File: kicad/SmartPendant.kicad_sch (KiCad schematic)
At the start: 52 parts, among them J1 UART, J2 ST-LINK, J3 Conn_01x05, J4 TYPE-C16PIN, J5 Display, Q2 MMBT3904, U1 WEACT BLACKPILL F4X1, U2 AMS1117-3.3, U3 MB85RC256VPNF

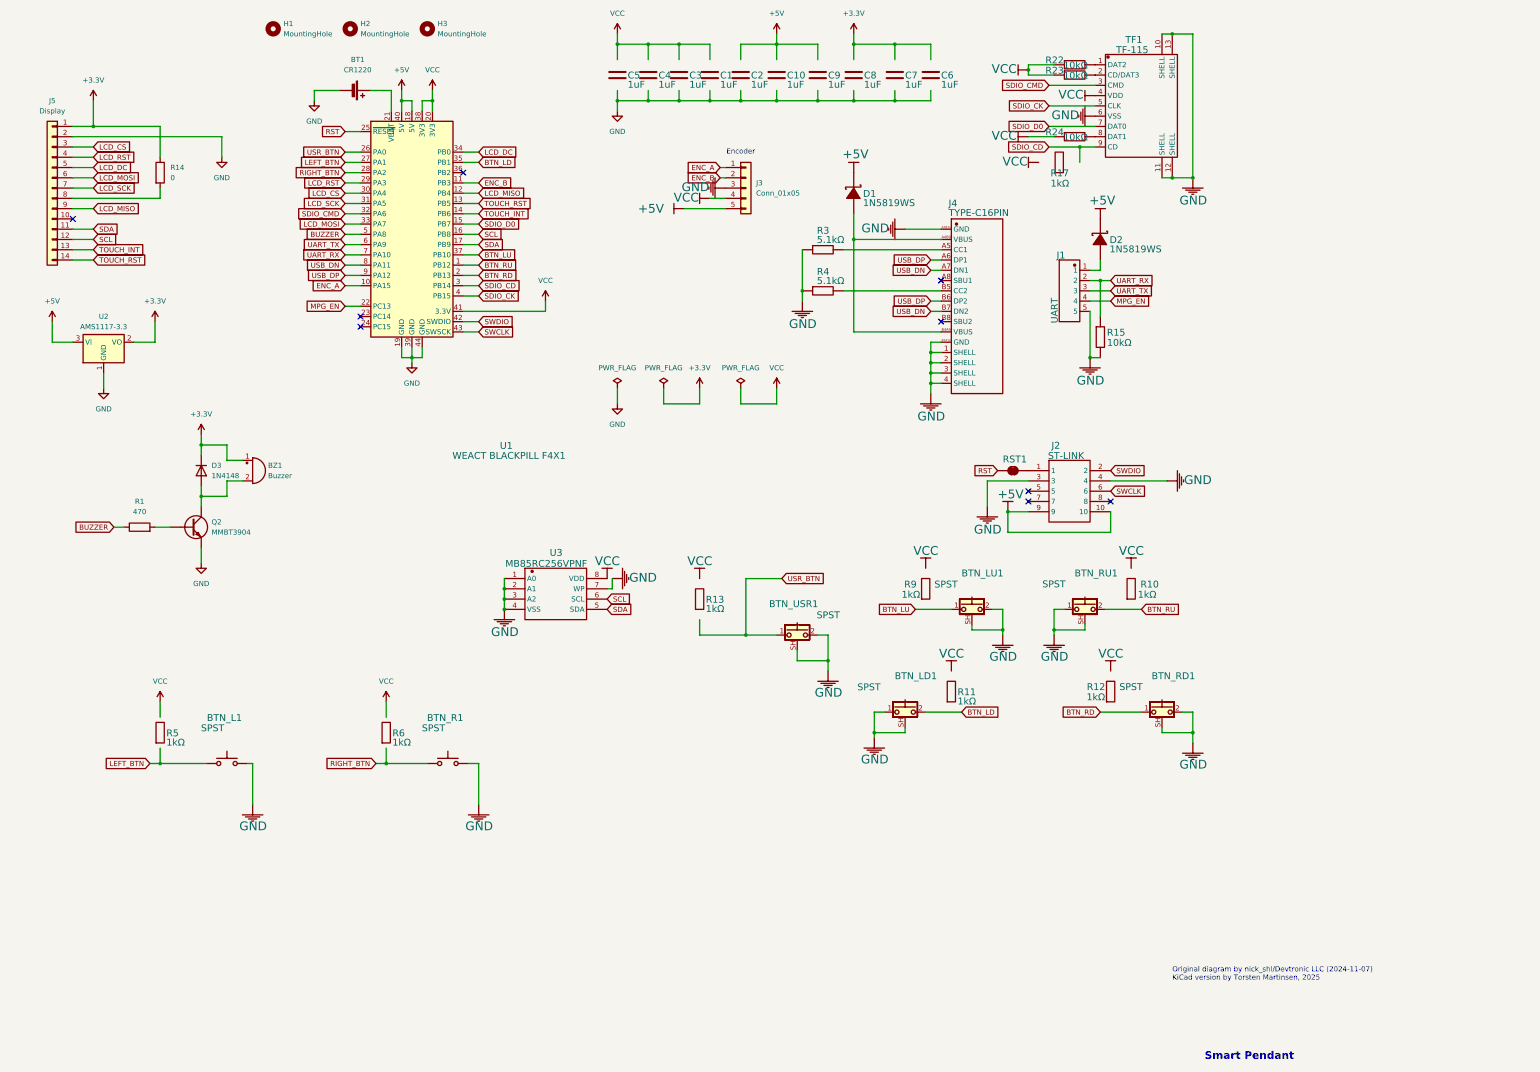
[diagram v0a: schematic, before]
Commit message: Update rest of power symbols.
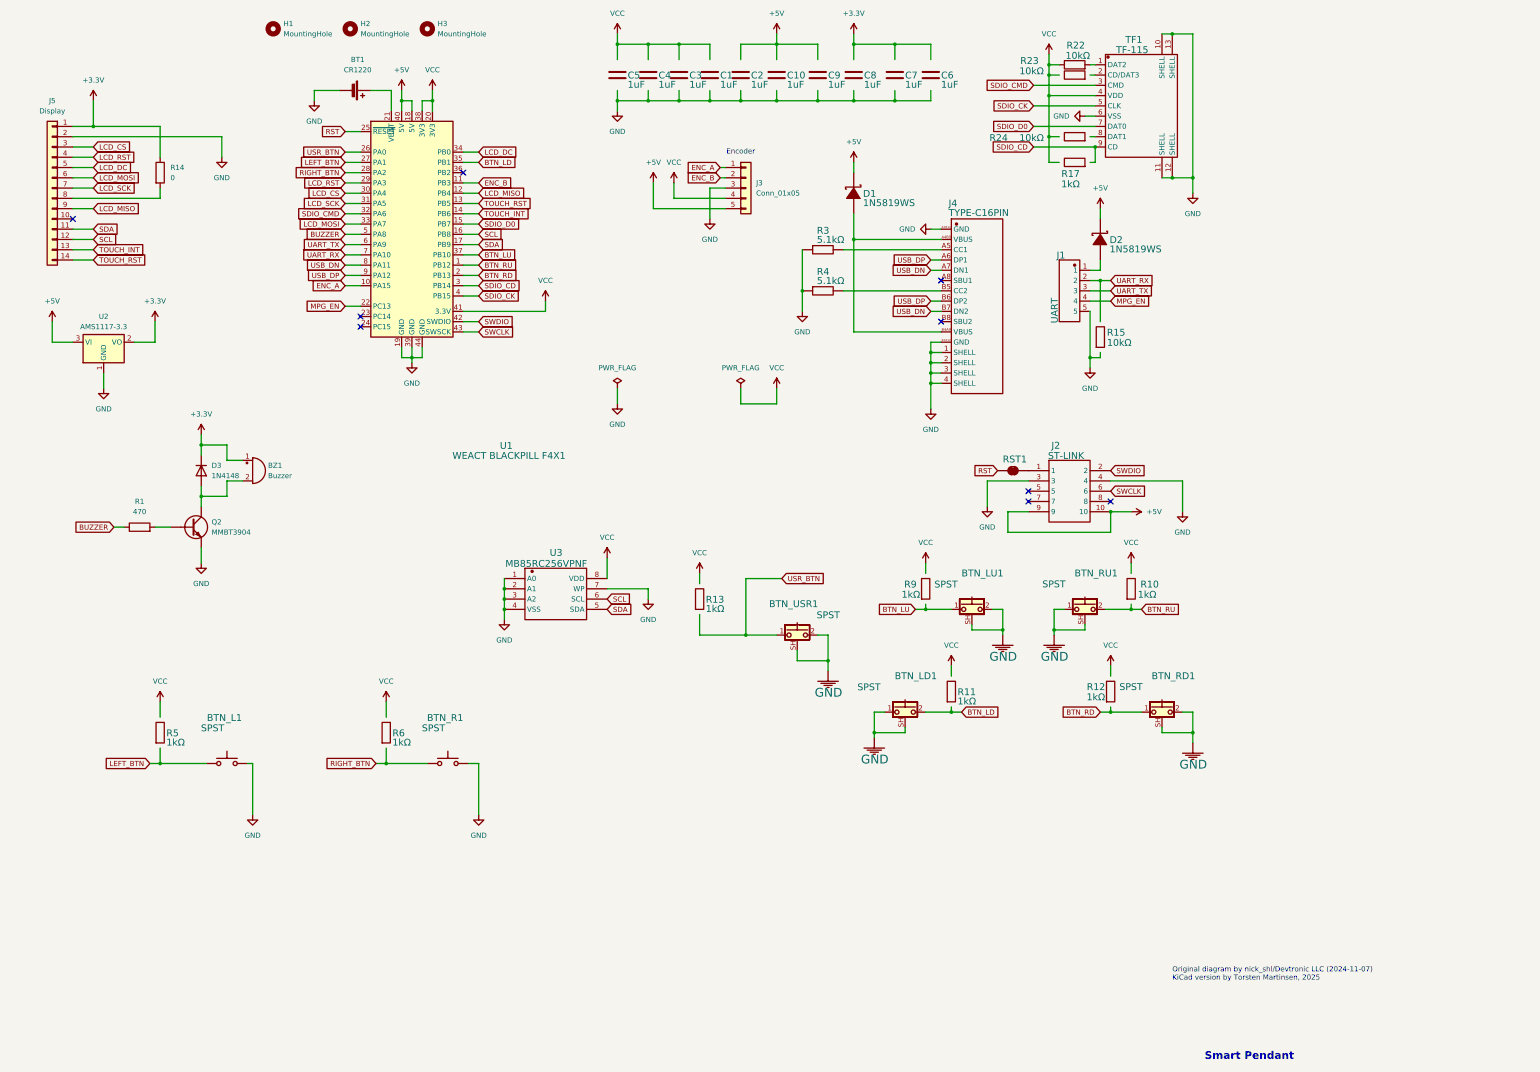
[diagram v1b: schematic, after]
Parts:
- R15: symbol 0805W8F1002T5E_13 -> Device:R
- R22: symbol 0805W8F1002T5E_14 -> Device:R
- R23: symbol 0805W8F1002T5E_15 -> Device:R
- R24: symbol 0805W8F1002T5E_16 -> Device:R
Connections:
- net GND: no longer R15.2
- net UART_RX: no longer R15.1
- net VCC: no longer R23.1, R24.1
- net at TF1.8 (DAT1): no longer R24.2
- net at TF1.2 (CD/DAT3): no longer R23.2
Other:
- moved on the sheet: R17

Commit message: Add footprints, initial outline.
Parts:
- removed H3: MountingHole, MountingHole:MountingHole_3.2mm_M3, symbol Mechanical:MountingHole
- removed Q2: MMBT3904, symbol Device:Q_NPN
- added Q1: MMBT3904, Package_TO_SOT_SMD:SOT-23, symbol Transistor_BJT:MMBT3904
- BT1: footprint (none) -> Custom:CR1220_Battery_Holder
- J5: footprint Connector_PinSocket_2.54mm:PinSocket_1x14_P2.54mm_Vertical_SMD_Pin1Left -> Custom:PinSocket_1x14_P2.54mm_Vertical_SMD_Pin1Left_TH
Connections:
- net GND: now also Q1.2 (E)
- net at R1.2: now also Q1.1 (B)
- net at BZ1.2 (-), D3.2 (A): now also Q1.3 (C)
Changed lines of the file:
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@@
 	)
 	(symbol
-		(lib_id "Mechanical:MountingHole")
-		(at 118.11 22.86 0)
-		(unit 1)
-		(exclude_from_sim no)
-		(in_bom no)
-		(on_board yes)
-		(dnp no)
-		(fields_autoplaced yes)
-		(property "Reference" "H3"
-			(at 120.65 21.5899 0)
-			(effects
-				(font
-					(size 1.27 1.27)
-				)
-				(justify left)
-			)
-		)
-		(property "Value" "MountingHole"
-			(at 120.65 24.1299 0)
-			(effects
-				(font
-					(size 1.27 1.27)
-				)
-				(justify left)
-			)
-		)
-		(property "Footprint" "MountingHole:MountingHole_3.2mm_M3"
-			(at 118.11 22.86 0)
-			(effects
-				(font
-					(size 1.27 1.27)
-				)
-				(hide yes)
-			)
-		)
-		(property "Datasheet" "~"
-			(at 118.11 22.86 0)
-			(effects
-				(font
-					(size 1.27 1.27)
-				)
-				(hide yes)
-			)
-		)
-		(property "Description" "Mounting Hole without connection"
-			(at 118.11 22.86 0)
-			(effects
-				(font
-					(size 1.27 1.27)
-				)
-				(hide yes)
-			)
-		)
-		(instances
-			(project ""
-				(path "/78cb6519-38e9-49e2-a9df-0cb5fdb5035f"
-					(reference "H3")
-					(unit 1)
-				)
-			)
-		)
-	)
-	(symbol
 		(lib_id "TYPE-C16PIN")
 		(at 254 91.44 0)
@@
 	)
 	(symbol
-		(lib_id "Device:Q_NPN")
-		(at 59.69 146.05 0)
-		(unit 1)
-		(exclude_from_sim no)
-		(in_bom yes)
-		(on_board yes)
-		(dnp no)
-		(fields_autoplaced yes)
-		(property "Reference" "Q2"
-			(at 64.77 144.7799 0)
-			(effects
-				(font
-					(size 1.27 1.27)
-				)
-				(justify left)
-			)
-		)
-		(property "Value" "MMBT3904"
-			(at 64.77 147.3199 0)
-			(effects
-				(font
-					(size 1.27 1.27)
-				)
-				(justify left)
-			)
-		)
-		(property "Footprint" ""
-			(at 64.77 143.51 0)
-			(effects
-				(font
-					(size 1.27 1.27)
-				)
-				(hide yes)
-			)
-		)
-		(property "Datasheet" "~"
-			(at 59.69 146.05 0)
-			(effects
-				(font
-					(size 1.27 1.27)
-				)
-				(hide yes)
-			)
-		)
-		(property "Description" "NPN bipolar junction transistor"
-			(at 59.69 146.05 0)
-			(effects
-				(font
-					(size 1.27 1.27)
-				)
-				(hide yes)
-			)
-		)
-		(pin "C"
-		)
-		(pin "B"
-		)
-		(pin "E"
-		)
-		(instances
-			(project ""
-				(path "/78cb6519-38e9-49e2-a9df-0cb5fdb5035f"
-					(reference "Q2")
-					(unit 1)
-				)
-			)
-		)
-	)
-	(symbol
 		(lib_id "Device:R")
 		(at 278.13 49.53 90)
@@
 			)
 		)
-		(property "Footprint" "Connector_PinSocket_2.54mm:PinSocket_1x14_P2.54mm_Vertical_SMD_Pin1Left"
+		(property "Footprint" "Custom:PinSocket_1x14_P2.54mm_Vertical_SMD_Pin1Left_TH"
 			(at 25.4 62.23 0)
 			(effects
@@
 			)
 		)
-		(property "Footprint" ""
+		(property "Footprint" "Custom:CR1220_Battery_Holder"
 			(at 100.584 38.1 90)
 			(effects
@@
 					(unit 1)
 				)
+			)
+		)
+	)
+	(symbol
+		(lib_id "Transistor_BJT:MMBT3904")
+		(at 59.69 146.05 0)
+		(unit 1)
+		(exclude_from_sim no)
+		(in_bom yes)
+		(on_board yes)
+		(dnp no)
+		(fields_autoplaced yes)
+		(property "Reference" "Q1"
+			(at 64.77 144.7799 0)
+			(effects
+				(font
+					(size 1.27 1.27)
+				)
+				(justify left)
+			)
+		)
+		(property "Value" "MMBT3904"
+			(at 64.77 147.3199 0)
+			(effects
+				(font
+					(size 1.27 1.27)
+				)
+				(justify left)
+			)
+		)
+		(property "Footprint" "Package_TO_SOT_SMD:SOT-23"
+			(at 64.77 147.955 0)
+			(effects
+				(font
+					(size 1.27 1.27)
+					(italic yes)
+				)
+				(justify left)
+				(hide yes)
+			)
+		)
+		(property "Datasheet" "https://www.onsemi.com/pdf/datasheet/pzt3904-d.pdf"
+			(at 59.69 146.05 0)
+			(effects
+				(font
+					(size 1.27 1.27)
+				)
+				(justify left)
+				(hide yes)
+			)
+		)
+		(property "Description" "0.2A Ic, 40V Vce, Small Signal NPN Transistor, SOT-23"
+			(at 59.69 146.05 0)
+			(effects
+				(font
+					(size 1.27 1.27)
+				)
+				(hide yes)
+			)
+		)
+		(pin "1"
+		)
+		(pin "3"
+		)
+		(pin "2"
+		)
+		(instances
+			(project ""
+				(path "/78cb6519-38e9-49e2-a9df-0cb5fdb5035f"
+					(reference "Q1")
+					(unit 1)
+				)

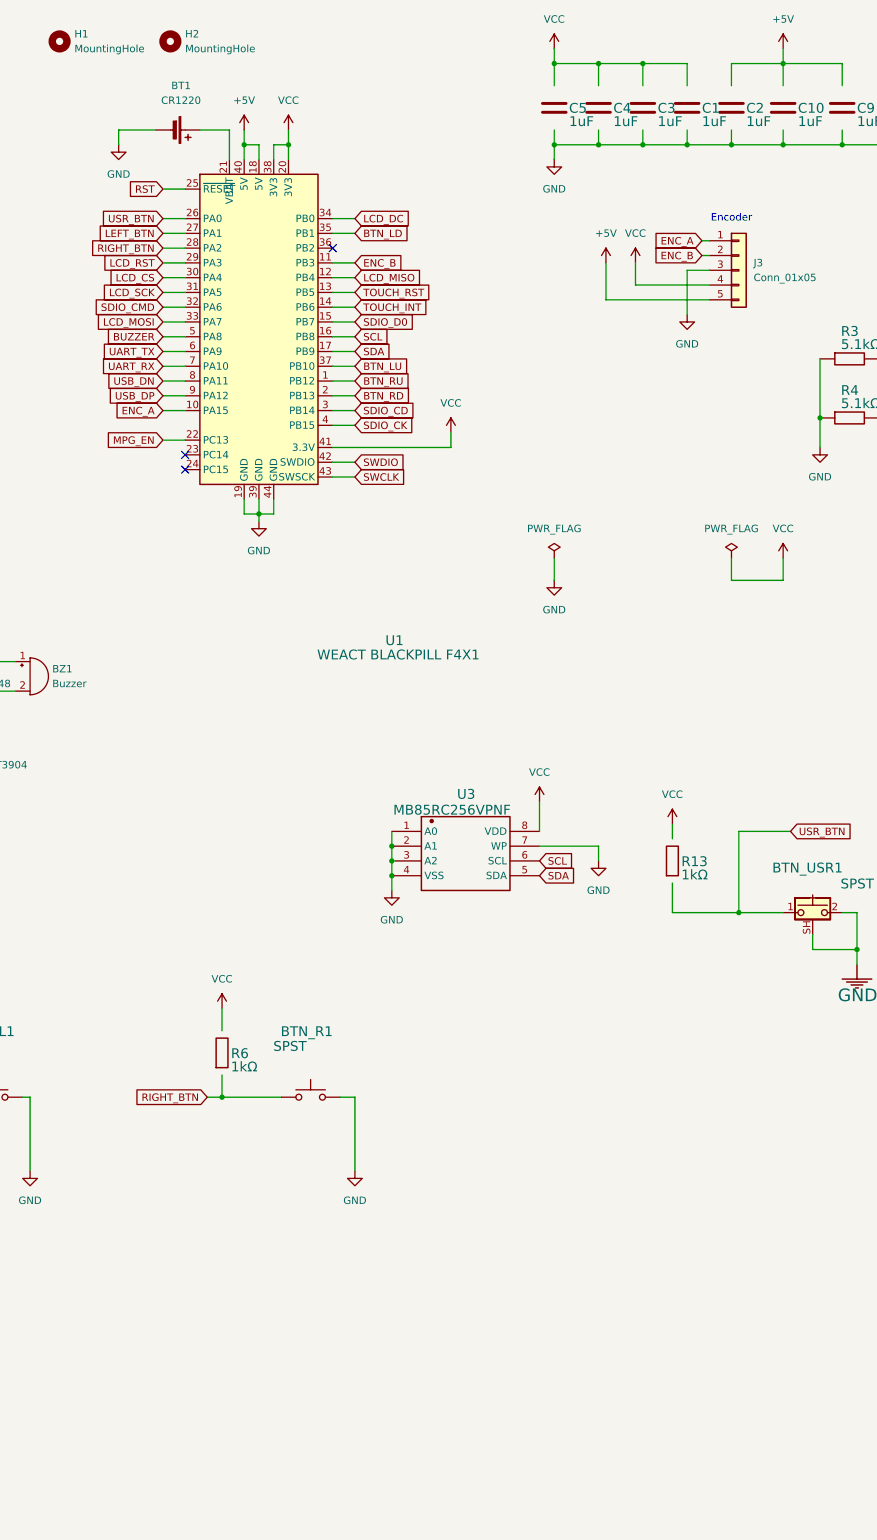
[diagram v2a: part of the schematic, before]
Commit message: Fix some footprint issues.
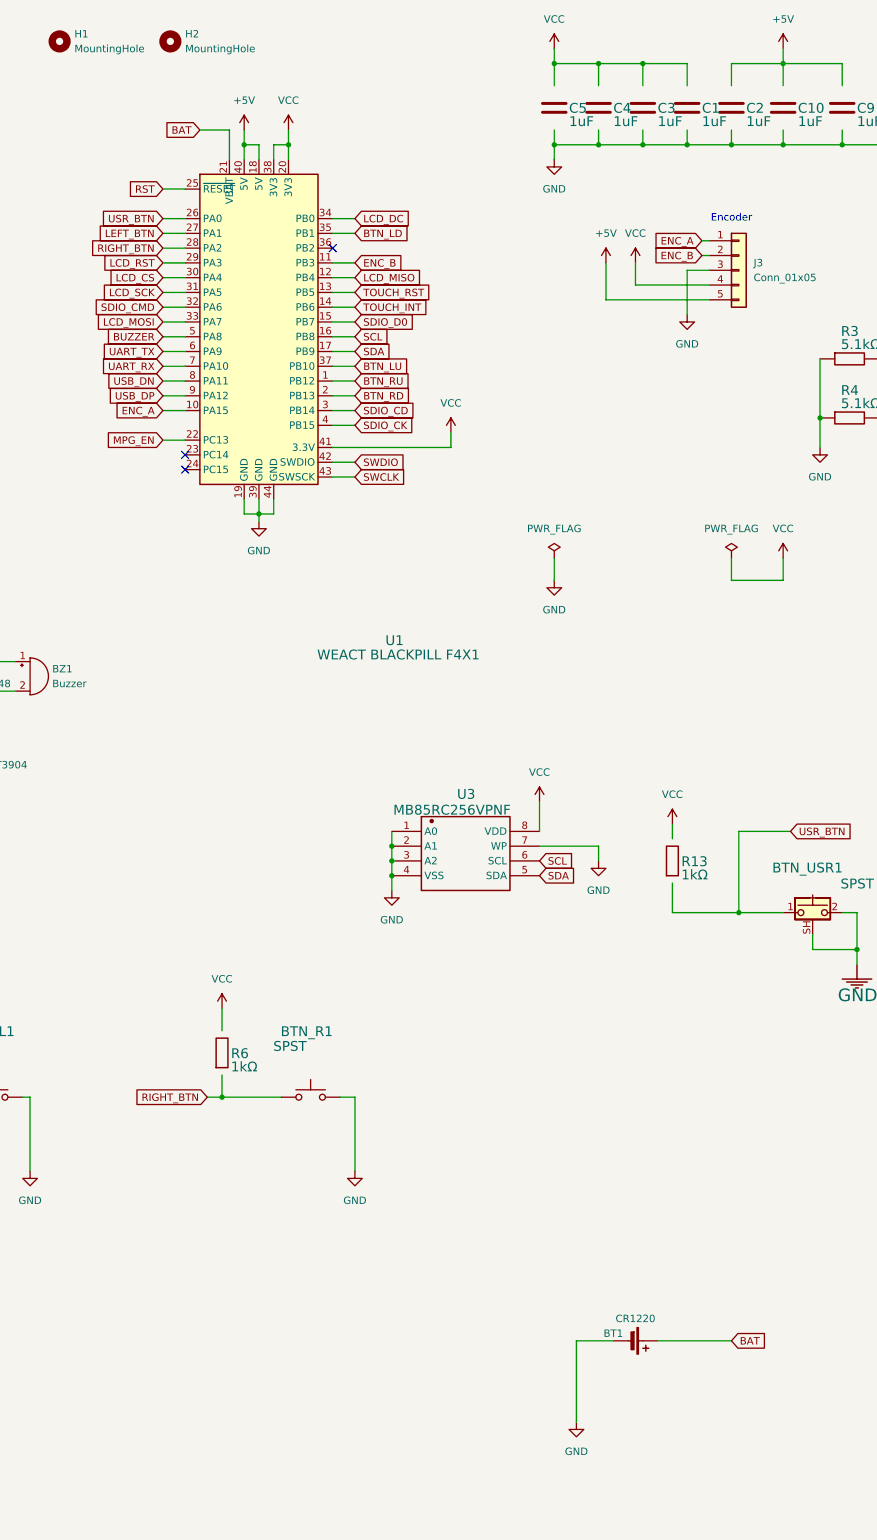
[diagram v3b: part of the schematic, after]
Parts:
- BTN_LD1, BTN_LU1, BTN_RD1, BTN_RU1, BTN_USR1: footprint SmartPendant:SMD_Push_Side_button_3x6x3.5mm -> Custom:SMD_Push_Side_button_3x6x3.5mm
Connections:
- net BAT: now reaches BT1.1 (+), U1.21 (VBAT)
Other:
- moved on the sheet: BT1
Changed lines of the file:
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@@
 	(wire
 		(pts
+			(xy 182.88 246.38) (xy 195.58 246.38)
+		)
+		(stroke
+			(width 0)
+			(type default)
+		)
+	)
+	(wire
+		(pts
 			(xy 307.34 59.69) (xy 302.26 59.69)
 		)
@@
 	(wire
 		(pts
-			(xy 90.17 38.1) (xy 90.17 40.64)
+			(xy 283.21 55.88) (xy 283.21 52.07)
 		)
 		(stroke
@@
 	(wire
 		(pts
-			(xy 283.21 55.88) (xy 283.21 52.07)
+			(xy 114.3 104.14) (xy 114.3 105.41)
 		)
 		(stroke
@@
 	(wire
 		(pts
-			(xy 114.3 104.14) (xy 114.3 105.41)
+			(xy 287.02 142.24) (xy 287.02 147.32)
 		)
 		(stroke
@@
 	(wire
 		(pts
-			(xy 287.02 142.24) (xy 287.02 147.32)
+			(xy 245.11 100.33) (xy 242.57 100.33)
 		)
 		(stroke
@@
 	(wire
 		(pts
-			(xy 245.11 100.33) (xy 242.57 100.33)
+			(xy 137.16 166.37) (xy 137.16 168.91)
 		)
 		(stroke
@@
 	(wire
 		(pts
-			(xy 137.16 166.37) (xy 137.16 168.91)
+			(xy 35.56 46.99) (xy 30.48 46.99)
 		)
 		(stroke
@@
 	(wire
 		(pts
-			(xy 35.56 46.99) (xy 30.48 46.99)
+			(xy 168.91 246.38) (xy 168.91 260.35)
 		)
 		(stroke
@@
 	(wire
 		(pts
-			(xy 90.17 38.1) (xy 96.52 38.1)
+			(xy 168.91 246.38) (xy 175.26 246.38)
 		)
 		(stroke
@@
 		)
 	)
+	(global_label "BAT"
+		(shape input)
+		(at 104.14 38.1 180)
+		(fields_autoplaced yes)
+		(effects
+			(font
+				(size 1.27 1.27)
+			)
+			(justify right)
+		)
+		(property "Intersheetrefs" "${INTERSHEET_REFS}"
+			(at 97.8286 38.1 0)
+			(effects
+				(font
+					(size 1.27 1.27)
+				)
+				(justify right)
+				(hide yes)
+			)
+		)
+	)
 	(global_label "BUZZER"
 		(shape input)
@@
 		)
 	)
+	(global_label "BAT"
+		(shape input)
+		(at 195.58 246.38 0)
+		(fields_autoplaced yes)
+		(effects
+			(font
+				(size 1.27 1.27)
+			)
+			(justify left)
+		)
+		(property "Intersheetrefs" "${INTERSHEET_REFS}"
+			(at 201.8914 246.38 0)
+			(effects
+				(font
+					(size 1.27 1.27)
+				)
+				(justify left)
+				(hide yes)
+			)
+		)
+	)
 	(global_label "BTN_RD"
 		(shape input)
@@
 			)
 		)
-		(property "Footprint" "SmartPendant:SMD_Push_Side_button_3x6x3.5mm"
+		(property "Footprint" "Custom:SMD_Push_Side_button_3x6x3.5mm"
 			(at 252.73 161.29 0)
 			(effects
@@
 			)
 		)
-		(property "Footprint" "SmartPendant:SMD_Push_Side_button_3x6x3.5mm"
+		(property "Footprint" "Custom:SMD_Push_Side_button_3x6x3.5mm"
 			(at 209.55 167.64 0)
 			(effects
@@
 	(symbol
 		(lib_id "power:GND")
-		(at 90.17 40.64 0)
+		(at 168.91 260.35 0)
 		(unit 1)
 		(exclude_from_sim no)
@@
 		(fields_autoplaced yes)
 		(property "Reference" "#PWR06"
-			(at 90.17 46.99 0)
+			(at 168.91 266.7 0)
 			(effects
 				(font
@@
 		)
 		(property "Value" "GND"
-			(at 90.17 45.72 0)
+			(at 168.91 265.43 0)
 			(effects
 				(font
@@
 		)
 		(property "Footprint" ""
-			(at 90.17 40.64 0)
+			(at 168.91 260.35 0)
 			(effects
 				(font
@@
 		)
 		(property "Datasheet" ""
-			(at 90.17 40.64 0)
+			(at 168.91 260.35 0)
 			(effects
 				(font
@@
 		)
 		(property "Description" "Power symbol creates a global label with name \"GND\" , ground"
-			(at 90.17 40.64 0)
+			(at 168.91 260.35 0)
 			(effects
 				(font
@@
 			)
 		)
-		(property "Footprint" "SmartPendant:SMD_Push_Side_button_3x6x3.5mm"
+		(property "Footprint" "Custom:SMD_Push_Side_button_3x6x3.5mm"
 			(at 280.67 161.29 0)
 			(effects
@@
 			)
 		)
-		(property "Footprint" "SmartPendant:SMD_Push_Side_button_3x6x3.5mm"
+		(property "Footprint" "Custom:SMD_Push_Side_button_3x6x3.5mm"
 			(at 299.72 186.69 0)
 			(effects
@@
 	(symbol
 		(lib_id "Device:Battery_Cell")
-		(at 99.06 38.1 270)
+		(at 177.8 246.38 270)
 		(unit 1)
 		(exclude_from_sim no)
@@
 		(on_board yes)
 		(dnp no)
-		(fields_autoplaced yes)
 		(property "Reference" "BT1"
-			(at 100.9015 30.48 90)
+			(at 175.26 245.11 90)
 			(effects
 				(font
@@
 		)
 		(property "Value" "CR1220"
-			(at 100.9015 33.02 90)
+			(at 179.07 242.57 90)
 			(effects
 				(font
@@
 		)
 		(property "Footprint" "Custom:CR1220_Battery_Holder"
-			(at 100.584 38.1 90)
+			(at 179.324 246.38 90)
 			(effects
 				(font
@@
 		)
 		(property "Datasheet" "~"
-			(at 100.584 38.1 90)
+			(at 179.324 246.38 90)
 			(effects
 				(font
@@
 		)
 		(property "Description" "Single-cell battery"
-			(at 99.06 38.1 0)
+			(at 177.8 246.38 0)
 			(effects
 				(font
@@
 			)
 		)
-		(property "Footprint" "SmartPendant:SMD_Push_Side_button_3x6x3.5mm"
+		(property "Footprint" "Custom:SMD_Push_Side_button_3x6x3.5mm"
 			(at 236.22 186.69 0)
 			(effects
